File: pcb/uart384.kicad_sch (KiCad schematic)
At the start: 42 parts, among them IC1 ICE40LP384-SG32, J1 USB_A, J2 TC2050, J3 TC2050_ext, J4 Conn_02x07_Odd_Even, SW1 SW_Push, U1 AT25DF256-SSHN, U2 CP2102-QFN28, U3 MIC5365-1.2YC5, U4 AMS1117-2.5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

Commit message: optimize the shit out of the PCB because I'm bored.
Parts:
- removed JP1: VSEL2, Jumper:SolderJumper-3_P1.3mm_Bridged2Bar12_RoundedPad1.0x1.5mm, symbol Jumper:SolderJumper_3_Bridged12
- added JP2: VSEL2, Jumper:SolderJumper-3_P1.3mm_Open_RoundedPad1.0x1.5mm, symbol Jumper:SolderJumper_3_Open
- renumbered JP2 to JP1
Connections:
- net +2V5: now also JP2.1 (A)
- net at U4.2 (VO), U5.2 (VO): now also JP2.3 (B)
- net at JP1.3 (B): now also JP2.2 (C)
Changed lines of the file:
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@@
 		(dnp no)
 		(fields_autoplaced yes)
-		(property "Reference" "JP2"
+		(property "Reference" "JP1"
 			(at 293.37 48.26 0)
 			(effects
@@
 			(project ""
 				(path "/951aeac3-6c61-42a5-aa61-f58713889333"
-					(reference "JP2")
+					(reference "JP1")
 					(unit 1)
 				)
@@
 	)
 	(symbol
-		(lib_id "Jumper:SolderJumper_3_Bridged12")
-		(at 285.75 64.77 180)
-		(unit 1)
-		(exclude_from_sim no)
-		(in_bom no)
-		(on_board yes)
-		(dnp no)
-		(property "Reference" "JP1"
-			(at 285.75 68.58 0)
-			(effects
-				(font
-					(size 1.27 1.27)
-				)
-			)
-		)
-		(property "Value" "VSEL2"
-			(at 285.75 71.12 0)
-			(effects
-				(font
-					(size 1.27 1.27)
-				)
-			)
-		)
-		(property "Footprint" "Jumper:SolderJumper-3_P1.3mm_Bridged2Bar12_RoundedPad1.0x1.5mm"
-			(at 285.75 64.77 0)
-			(effects
-				(font
-					(size 1.27 1.27)
-				)
-				(hide yes)
-			)
-		)
-		(property "Datasheet" "~"
-			(at 285.75 64.77 0)
-			(effects
-				(font
-					(size 1.27 1.27)
-				)
-				(hide yes)
-			)
-		)
-		(property "Description" "3-pole Solder Jumper, pins 1+2 closed/bridged"
-			(at 285.75 64.77 0)
-			(effects
-				(font
-					(size 1.27 1.27)
-				)
-				(hide yes)
-			)
-		)
-		(pin "2"
-		)
-		(pin "1"
-		)
-		(pin "3"
-		)
-		(instances
-			(project "uart384"
-				(path "/951aeac3-6c61-42a5-aa61-f58713889333"
-					(reference "JP1")
-					(unit 1)
-				)
-			)
-		)
-	)
-	(symbol
 		(lib_id "Device:C")
 		(at 64.77 173.99 90)
@@
 					(unit 1)
 				)
+			)
+		)
+	)
+	(symbol
+		(lib_id "Jumper:SolderJumper_3_Open")
+		(at 285.75 64.77 180)
+		(unit 1)
+		(exclude_from_sim no)
+		(in_bom no)
+		(on_board yes)
+		(dnp no)
+		(fields_autoplaced yes)
+		(property "Reference" "JP2"
+			(at 285.75 68.58 0)
+			(effects
+				(font
+					(size 1.27 1.27)
+				)
+			)
+		)
+		(property "Value" "VSEL2"
+			(at 285.75 71.12 0)
+			(effects
+				(font
+					(size 1.27 1.27)
+				)
+			)
+		)
+		(property "Footprint" "Jumper:SolderJumper-3_P1.3mm_Open_RoundedPad1.0x1.5mm"
+			(at 285.75 64.77 0)
+			(effects
+				(font
+					(size 1.27 1.27)
+				)
+				(hide yes)
+			)
+		)
+		(property "Datasheet" "~"
+			(at 285.75 64.77 0)
+			(effects
+				(font
+					(size 1.27 1.27)
+				)
+				(hide yes)
+			)
+		)
+		(property "Description" "Solder Jumper, 3-pole, open"
+			(at 285.75 64.77 0)
+			(effects
+				(font
+					(size 1.27 1.27)
+				)
+				(hide yes)
+			)
+		)
+		(pin "3"
+		)
+		(pin "1"
+		)
+		(pin "2"
+		)
+		(instances
+			(project ""
+				(path "/951aeac3-6c61-42a5-aa61-f58713889333"
+					(reference "JP2")
+					(unit 1)
+				)

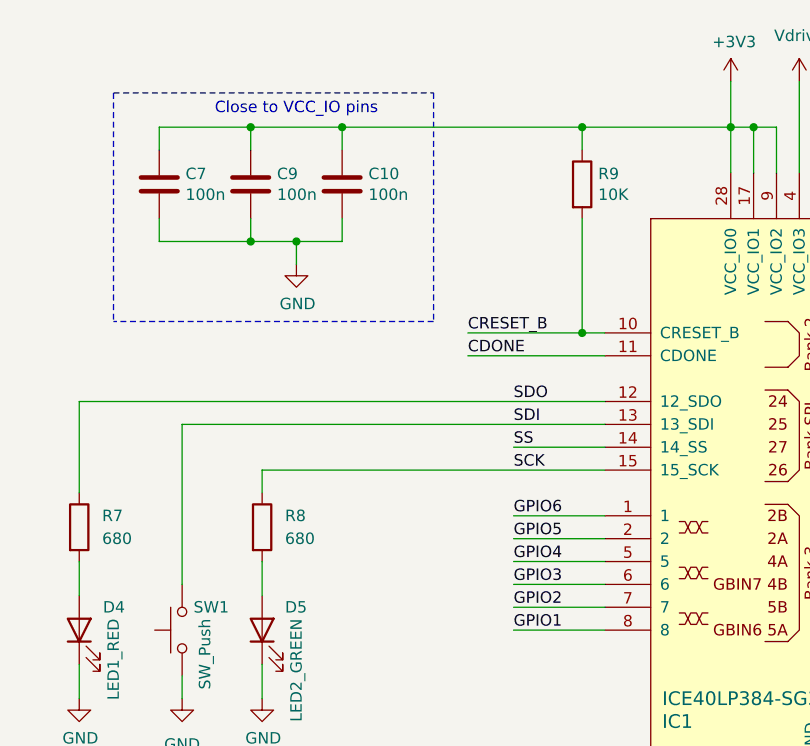
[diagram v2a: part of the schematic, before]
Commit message: PCB: add in-line resistor to switch SW1 to avoid possible shorts.
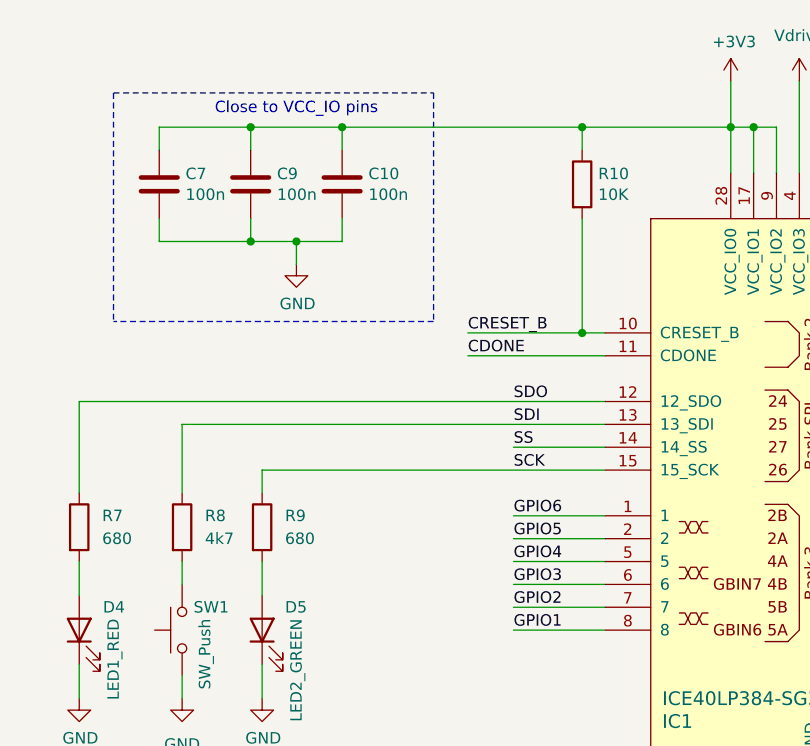
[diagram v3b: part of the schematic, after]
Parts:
- added R8: 4k7, Resistor_SMD:R_0603_1608Metric, symbol Device:R
- renumbered R9 to R10, R8 to R9
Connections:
- net SDI: now also R8.1; no longer SW1.2
- new net: R8.2, SW1.2
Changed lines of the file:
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@@
 	(wire
 		(pts
+			(xy 219.71 156.21) (xy 219.71 163.83)
+		)
+		(stroke
+			(width 0)
+			(type default)
+		)
+	)
+	(wire
+		(pts
 			(xy 38.1 252.73) (xy 38.1 250.19)
 		)
@@
 	(wire
 		(pts
-			(xy 219.71 156.21) (xy 219.71 173.99)
-		)
-		(stroke
-			(width 0)
-			(type default)
-		)
-	)
-	(wire
-		(pts
 			(xy 102.87 36.83) (xy 102.87 39.37)
 		)
@@
 	(wire
 		(pts
+			(xy 219.71 171.45) (xy 219.71 173.99)
+		)
+		(stroke
+			(width 0)
+			(type default)
+		)
+	)
+	(wire
+		(pts
 			(xy 317.5 156.21) (xy 328.93 156.21)
 		)
@@
 		(dnp no)
 		(fields_autoplaced yes)
-		(property "Reference" "R8"
+		(property "Reference" "R9"
 			(at 231.14 166.3699 0)
 			(effects
@@
 			(project ""
 				(path "/951aeac3-6c61-42a5-aa61-f58713889333"
-					(reference "R8")
+					(reference "R9")
 					(unit 1)
 				)
@@
 		(on_board yes)
 		(dnp no)
-		(property "Reference" "R9"
+		(property "Reference" "R10"
 			(at 265.938 128.3716 0)
 			(effects
@@
 			(project "uart384"
 				(path "/951aeac3-6c61-42a5-aa61-f58713889333"
-					(reference "R9")
+					(reference "R10")
 					(unit 1)
 				)
@@
 					(unit 1)
 				)
+			)
+		)
+	)
+	(symbol
+		(lib_id "Device:R")
+		(at 219.71 167.64 0)
+		(unit 1)
+		(exclude_from_sim no)
+		(in_bom yes)
+		(on_board yes)
+		(dnp no)
+		(fields_autoplaced yes)
+		(property "Reference" "R8"
+			(at 222.25 166.3699 0)
+			(effects
+				(font
+					(size 1.27 1.27)
+				)
+				(justify left)
+			)
+		)
+		(property "Value" "4k7"
+			(at 222.25 168.9099 0)
+			(effects
+				(font
+					(size 1.27 1.27)
+				)
+				(justify left)
+			)
+		)
+		(property "Footprint" "Resistor_SMD:R_0603_1608Metric"
+			(at 217.932 167.64 90)
+			(effects
+				(font
+					(size 1.27 1.27)
+				)
+				(hide yes)
+			)
+		)
+		(property "Datasheet" "~"
+			(at 219.71 167.64 0)
+			(effects
+				(font
+					(size 1.27 1.27)
+				)
+				(hide yes)
+			)
+		)
+		(property "Description" "Resistor"
+			(at 219.71 167.64 0)
+			(effects
+				(font
+					(size 1.27 1.27)
+				)
+				(hide yes)
+			)
+		)
+		(pin "2"
+		)
+		(pin "1"
+		)
+		(instances
+			(project "uart384"
+				(path "/951aeac3-6c61-42a5-aa61-f58713889333"
+					(reference "R8")
+					(unit 1)
+				)

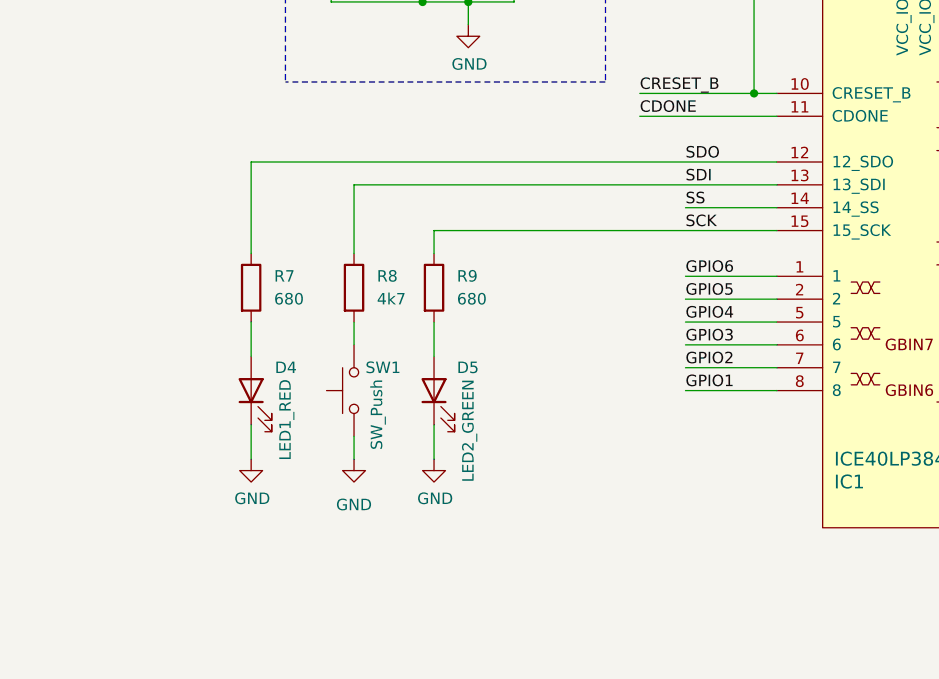
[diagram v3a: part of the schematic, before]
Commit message: add test-pads for easy access to differential pair GPIO1/GPIO2
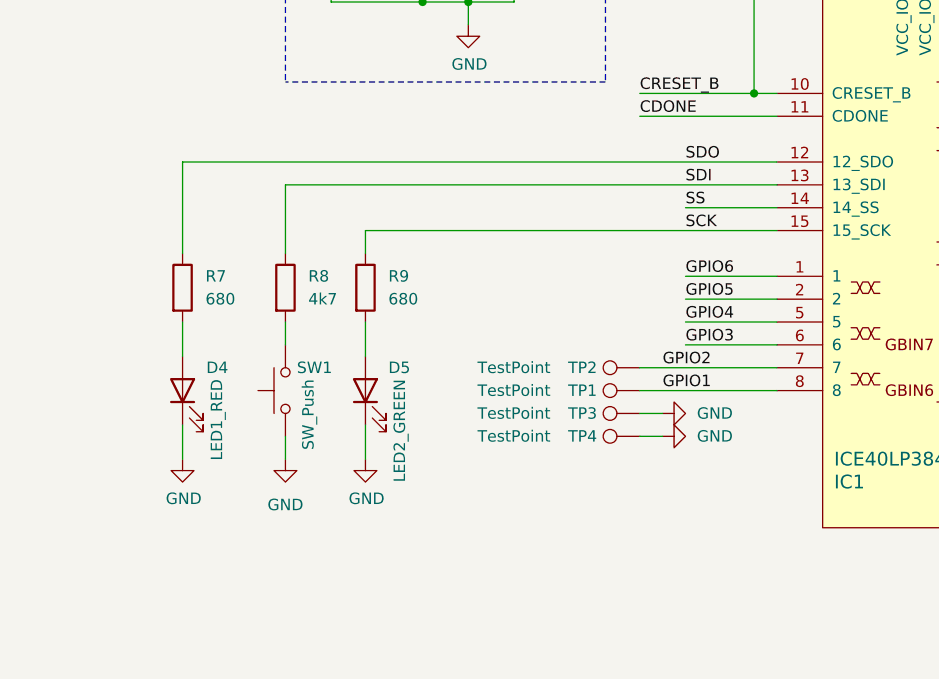
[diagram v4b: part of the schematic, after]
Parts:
- added TP1, TP2, TP3, TP4: TestPoint, TestPoint:TestPoint_Pad_1.0x1.0mm, symbol Connector:TestPoint
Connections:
- net GND: now also TP3.1, TP4.1
- net GPIO1: now also TP1.1
- net GPIO2: now also TP2.1
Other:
- moved on the sheet: D4, D5, R7, R8, R9, SW1

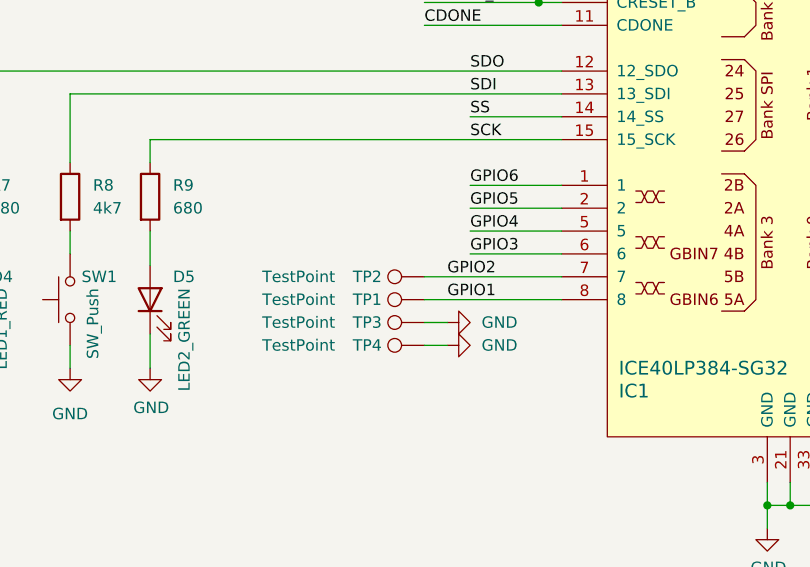
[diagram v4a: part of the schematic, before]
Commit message: PCB: add test-pads for easy access to differential pair GPIO5/GPIO6
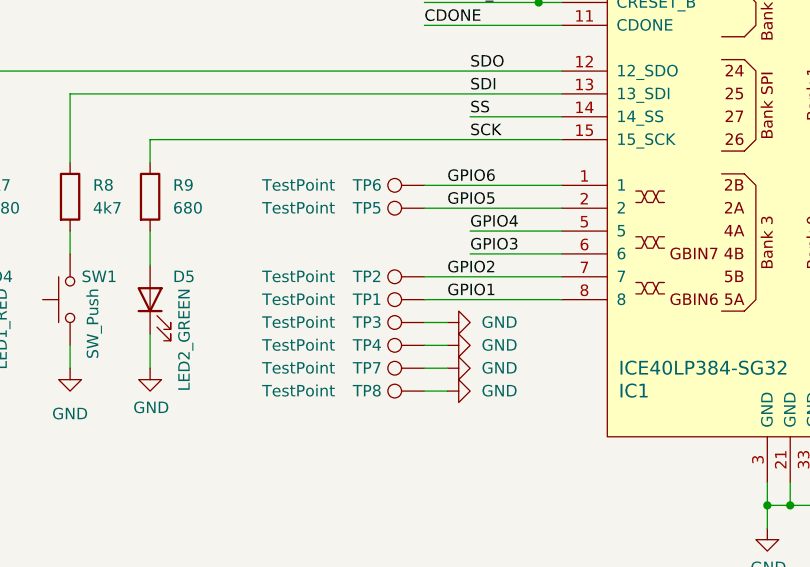
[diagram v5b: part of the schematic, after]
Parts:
- added TP5, TP6, TP7, TP8: TestPoint, TestPoint:TestPoint_Pad_1.0x1.0mm, symbol Connector:TestPoint
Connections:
- net GND: now also TP7.1, TP8.1
- net GPIO5: now also TP5.1
- net GPIO6: now also TP6.1
